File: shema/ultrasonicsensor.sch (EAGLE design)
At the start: 17 parts, among them IC1 PIC12F675P, IC2 78L05Z, T1 BC547, X1 C-GRID-05-70543

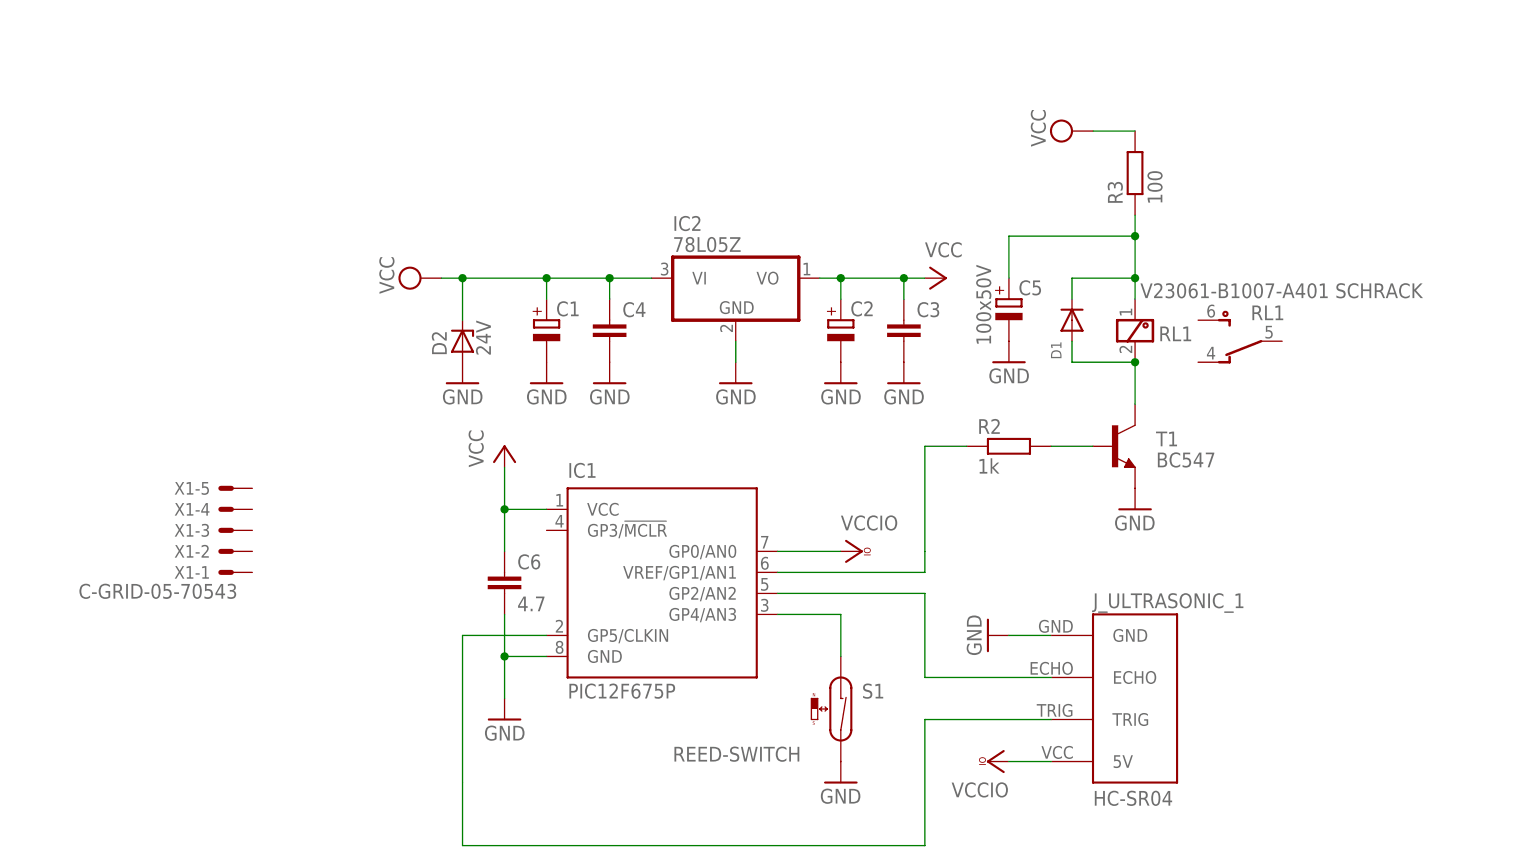
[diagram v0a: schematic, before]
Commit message: added power control of usound module
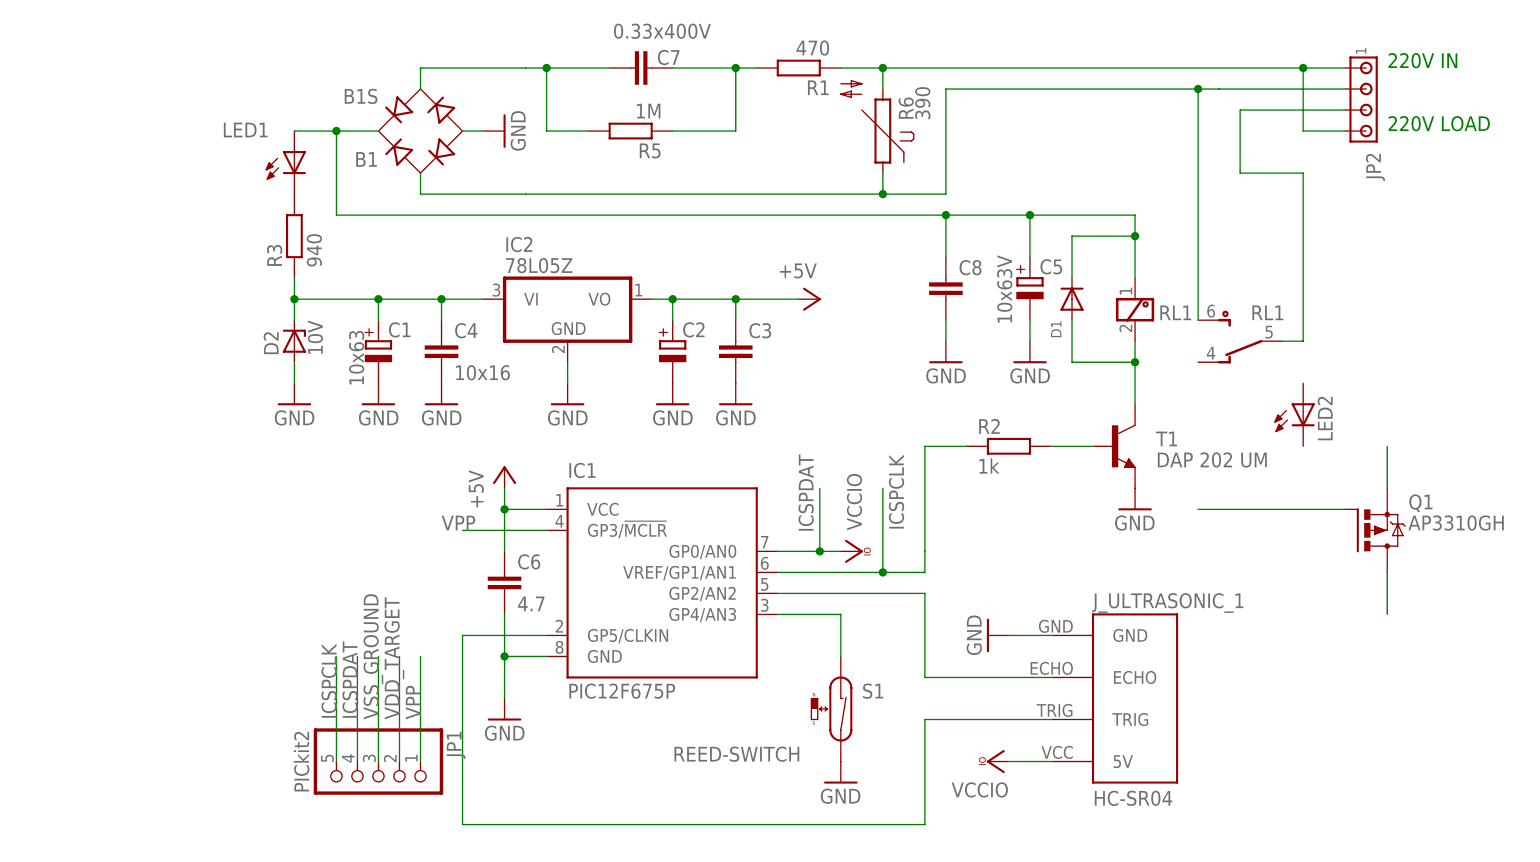
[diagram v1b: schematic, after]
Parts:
- removed X1: C-GRID-05-70543, con-molex:C-GRID-05-70543
- added B1: B1S, rectifier:B1S
- added C7: 0.33x400V, rcl:C-EU025-030X050
- added C8: (no value), rcl:C-EU025-030X050
- added JP1: PICkit2, pinhead:PINHD-1X5
- added JP2: (no value), con-amp:MTA04-156
- added LED1, LED2: (no value), led:LED3MM
- added R1: 470, rcl:R-EU_0207/2V
- added R5: 1M, rcl:R-EU_0207/2V
- added R6: 390, varistor:S14K385
- C1: value (none) -> 10x63
- C4: value (none) -> 10x16
- C5: value 100x50V -> 10x63V
- D2: value 24V -> 10V
- R3: value 100 -> 940
- T1: value BC547 -> DAP 202 UM
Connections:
- removed net N$4: IC1.VREF/GP1/AN1, R2.1
- removed net N$9 (its old number): C5.+, D1.C, R3.1, RL1K.1
- new net +24V: C1.+, C4.1, D2.C, IC2.VI, R3.1
- new net 220-1: JP2.1, JP2.4, R1.1, R6.2
- new net 220-2: B1.AC1, JP2.2, R6.1, RL1K1.6
- new net 220-LOAD: JP2.3, RL1K1.5
- new net ICSPCLK: IC1.VREF/GP1/AN1, JP1.5, R2.1
- new net ICSPDAT: IC1.GP0/AN0, JP1.4
- new net N$10: LED1.C, R3.2
- new net N$12: C7.1, R1.2, R5.1
- new net N$13: B1.AC2, C7.2, R5.2
- new net N$5: B1.+, C5.+, C8.1, D1.C, LED1.A, RL1K.1
- new net VDD_TARGET: JP1.2
- new net VPP: IC1.GP3/!MCLR, JP1.1
- new net VSS_GROUND: JP1.3
- net GND: now also B1.-, C8.2
- net VCC: no longer C1.+, C4.1, D2.C, IC2.VI, R3.2
- net VCCIO: no longer IC1.GP0/AN0
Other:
- note added: "220V IN"
- note added: "220V LOAD"
- moved on the sheet: C1, C2, C3, C4, C5, D1, D2, IC2, R3, RL1
